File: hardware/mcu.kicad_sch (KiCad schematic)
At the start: 11 parts, among them U0 STM32U575CIT6

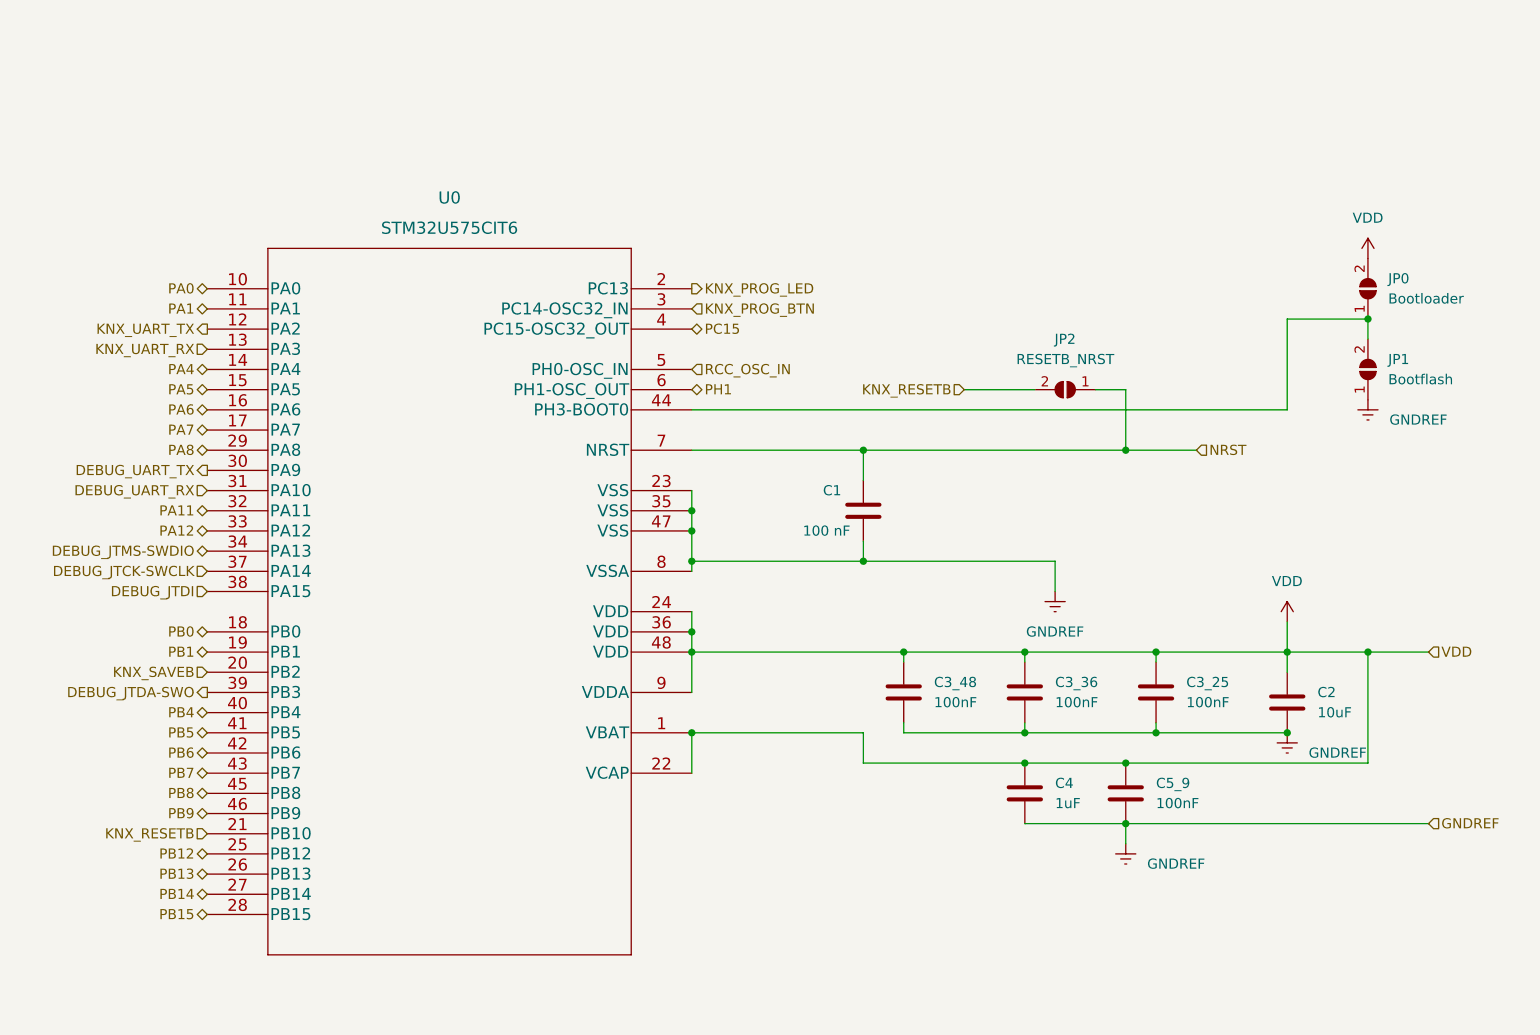
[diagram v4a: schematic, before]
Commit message: Switch to STM32G491KEU6 with NCN5130
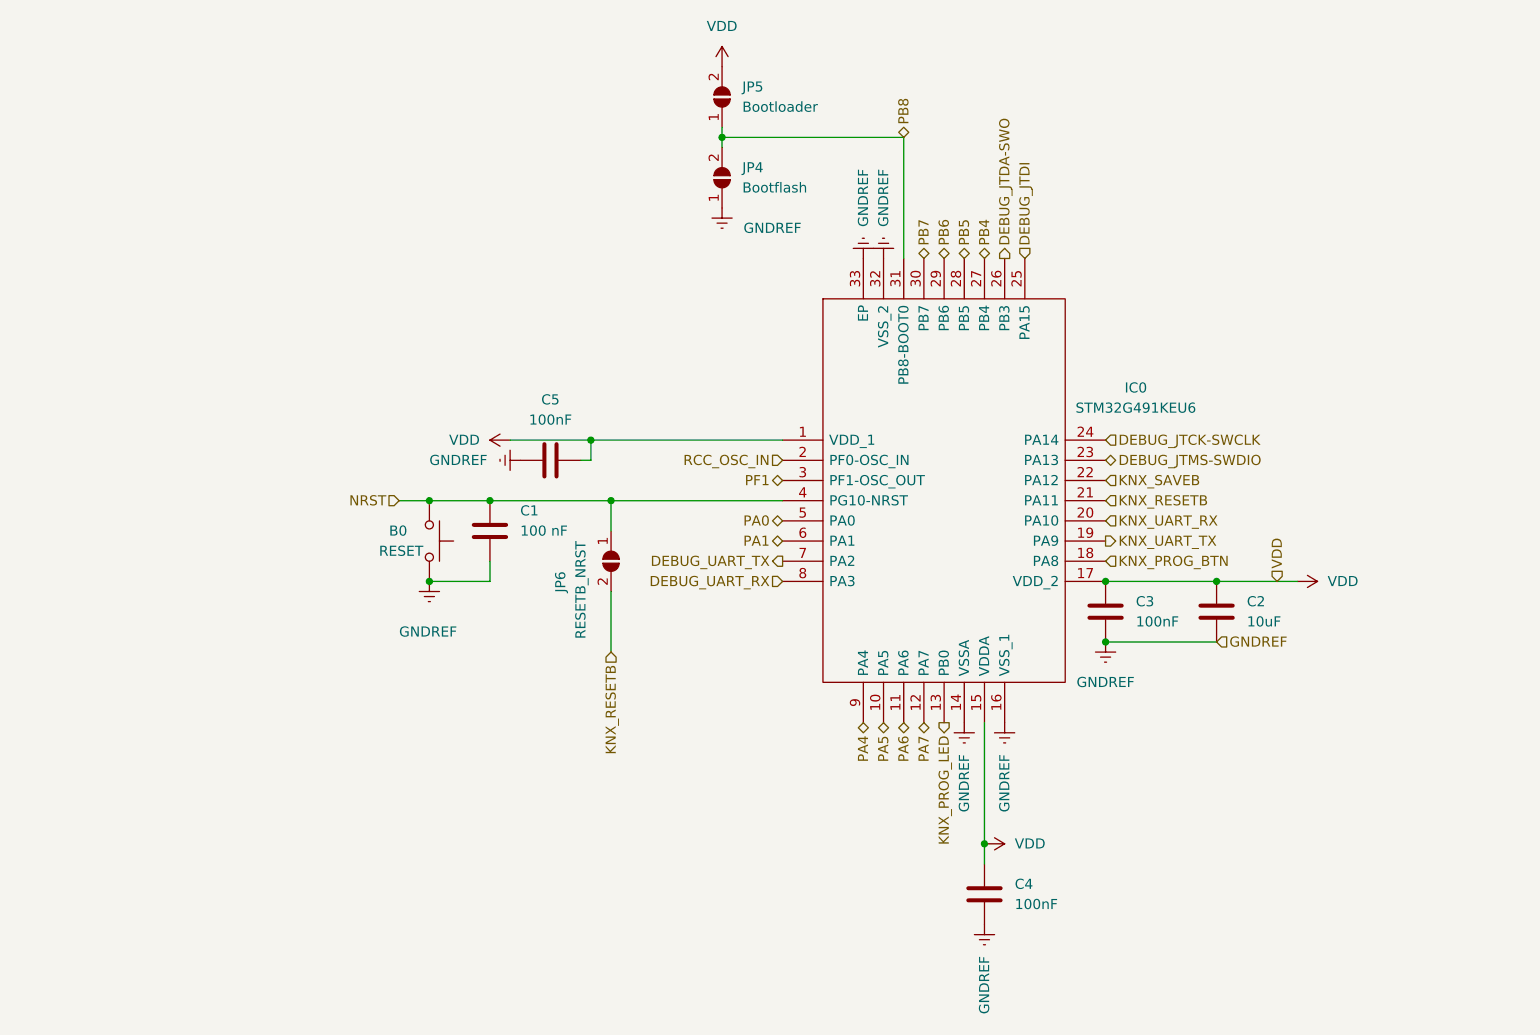
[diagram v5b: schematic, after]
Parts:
- removed C4: 1uF, Capacitor_SMD:C_0603_1608Metric_Pad1.08x0.95mm_HandSolder, symbol Device:C
- removed C5_9: 100nF, Capacitor_SMD:C_0603_1608Metric_Pad1.08x0.95mm_HandSolder, symbol Device:C
- removed JP0: Bootloader, Jumper:SolderJumper-2_P1.3mm_Open_TrianglePad1.0x1.5mm, symbol Jumper:SolderJumper_2_Open
- removed JP1: Bootflash, Jumper:SolderJumper-2_P1.3mm_Open_TrianglePad1.0x1.5mm, symbol Jumper:SolderJumper_2_Open
- removed JP2: RESETB_NRST, Jumper:SolderJumper-2_P1.3mm_Open_TrianglePad1.0x1.5mm, symbol Jumper:SolderJumper_2_Open
- removed U0: STM32U575CIT6, KnxBoard:STM32U575CIT6, symbol STM32U575CIT6:STM32U575CIT6
- added B0: RESET, Button_Switch_SMD:SW_SPST_SKQG_WithStem, symbol Switch:SW_Push
- added IC0: STM32G491KEU6, QFN50P500X500X60-33N-D, symbol STM32G491KEU6:STM32G491KEU6
- added JP4: Bootflash, Jumper:SolderJumper-2_P1.3mm_Open_TrianglePad1.0x1.5mm, symbol Jumper:SolderJumper_2_Open
- added JP5: Bootloader, Jumper:SolderJumper-2_P1.3mm_Open_TrianglePad1.0x1.5mm, symbol Jumper:SolderJumper_2_Open
- added JP6: RESETB_NRST, Jumper:SolderJumper-2_P1.3mm_Open_TrianglePad1.0x1.5mm, symbol Jumper:SolderJumper_2_Open
- renumbered C3_48 to C3, C3_36 to C4, C3_25 to C5
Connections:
- net DEBUG_JTCK-SWCLK: now also IC0.24 (PA14)
- net DEBUG_JTDA-SWO: now also IC0.26 (PB3)
- net DEBUG_JTDI: now also IC0.25 (PA15)
- net DEBUG_JTMS-SWDIO: now also IC0.23 (PA13)
- net DEBUG_UART_RX: now also IC0.8 (PA3)
- net DEBUG_UART_TX: now also IC0.7 (PA2)
- net GNDREF: now also C5.1, B0.2, IC0.14 (VSSA), IC0.16 (VSS_1), IC0.32 (VSS_2), IC0.33 (EP), JP4.1 (A); no longer C5.2
- net KNX_PROG_BTN: now also IC0.18 (PA8)
- net KNX_PROG_LED: now also IC0.13 (PB0)
- net KNX_RESETB: now also IC0.21 (PA11), JP6.2 (B)
- net KNX_SAVEB: now also IC0.22 (PA12)
- net KNX_UART_RX: now also IC0.20 (PA10)
- net KNX_UART_TX: now also IC0.19 (PA9)
- net NRST: now also B0.1, IC0.4 (PG10-NRST), JP6.1 (A)
- net PA0: now also IC0.5 (PA0)
- net PA1: now also IC0.6 (PA1)
- net PA4: now also IC0.9 (PA4)
- net PA5: now also IC0.10 (PA5)
- net PA6: now also IC0.11 (PA6)
- net PA7: now also IC0.12 (PA7)
- net PB4: now also IC0.27 (PB4)
- net PB5: now also IC0.28 (PB5)
- net PB6: now also IC0.29 (PB6)
- net PB7: now also IC0.30 (PB7)
- net PB8: now also IC0.31 (PB8-BOOT0), JP4.2 (B), JP5.1 (A)
- net RCC_OSC_IN: now also IC0.2 (PF0-OSC_IN)
- net VDD: now also C5.2, IC0.1 (VDD_1), IC0.15 (VDDA), IC0.17 (VDD_2), JP5.2 (B); no longer C5.1
- new net PF1: IC0.3 (PF1-OSC_OUT)
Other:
- moved on the sheet: C2, C3, C4, C5

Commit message: Routage OK need check and mass and texts
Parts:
- removed JP4: Bootflash, Jumper:SolderJumper-2_P1.3mm_Open_TrianglePad1.0x1.5mm, symbol Jumper:SolderJumper_2_Open
- removed JP5: Bootloader, Jumper:SolderJumper-2_P1.3mm_Open_TrianglePad1.0x1.5mm, symbol Jumper:SolderJumper_2_Open
- added JP4: BootMode, Jumper:SolderJumper-3_P1.3mm_Open_RoundedPad1.0x1.5mm, symbol Jumper:SolderJumper_3_Bridged12
- renumbered C1 to C20, C5 to C21, C3 to C22, C2 to C23, C4 to C24
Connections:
- net GNDREF: now also JP4.1 (A)
- net PB8: now also JP4.2 (C)
- net VDD: now also JP4.3 (B)
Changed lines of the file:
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@@
   (junction (at 232.41 91.44) (diameter 0) (color 0 0 0 0)
   )
+  (junction (at 203.2 124.46) (diameter 0) (color 0 0 0 0)
+  )
   (junction (at 153.67 73.66) (diameter 0) (color 0 0 0 0)
   )
@@
   (junction (at 218.44 91.44) (diameter 0) (color 0 0 0 0)
   )
-  (junction (at 170.18 35.56) (diameter 0) (color 0 0 0 0)
-  )
   (junction (at 218.44 99.06) (diameter 0) (color 0 0 0 0)
   )
   (junction (at 140.97 81.28) (diameter 0) (color 0 0 0 0)
   )
-  (junction (at 203.2 124.46) (diameter 0) (color 0 0 0 0)
-  )
   (wire (pts (xy 129.54 81.28) (xy 133.35 81.28))
     (stroke (width 0) (type default) (color 0 0 0 0))
   )
-  (wire (pts (xy 170.18 34.29) (xy 170.18 35.56))
-    (stroke (width 0) (type default) (color 0 0 0 0))
-  )
   (wire (pts (xy 133.35 81.28) (xy 140.97 81.28))
     (stroke (width 0) (type default) (color 0 0 0 0))
@@
     (stroke (width 0) (type default) (color 0 0 0 0))
   )
-  (wire (pts (xy 170.18 35.56) (xy 170.18 36.83))
-    (stroke (width 0) (type default) (color 0 0 0 0))
-  )
-  (wire (pts (xy 193.04 35.56) (xy 170.18 35.56))
-    (stroke (width 0) (type default) (color 0 0 0 0))
-  )
   (wire (pts (xy 140.97 91.44) (xy 133.35 91.44))
     (stroke (width 0) (type default) (color 0 0 0 0))
   )
+  (wire (pts (xy 173.99 35.56) (xy 193.04 35.56))
+    (stroke (width 0) (type default) (color 0 0 0 0))
+  )
+  (wire (pts (xy 203.2 124.46) (xy 203.2 127))
+    (stroke (width 0) (type default) (color 0 0 0 0))
+  )
   (wire (pts (xy 140.97 88.9) (xy 140.97 91.44))
     (stroke (width 0) (type default) (color 0 0 0 0))
@@
     (stroke (width 0) (type default) (color 0 0 0 0))
   )
-  (wire (pts (xy 203.2 124.46) (xy 203.2 127))
+  (wire (pts (xy 203.2 109.22) (xy 203.2 124.46))
     (stroke (width 0) (type default) (color 0 0 0 0))
   )
@@
     (stroke (width 0) (type default) (color 0 0 0 0))
   )
-  (wire (pts (xy 203.2 109.22) (xy 203.2 124.46))
-    (stroke (width 0) (type default) (color 0 0 0 0))
-  )
   (wire (pts (xy 156.21 81.28) (xy 156.21 85.09))
     (stroke (width 0) (type default) (color 0 0 0 0))
@@
     (effects (font (size 1.27 1.27)) (justify left))
   )
-  (hierarchical_label "VDD" (shape input) (at 240.03 91.44 90)
-    (effects (font (size 1.27 1.27)) (justify left))
-  )
   (hierarchical_label "DEBUG_JTCK-SWCLK" (shape input) (at 218.44 73.66 0)
     (effects (font (size 1.27 1.27)) (justify left))
   )
-  (hierarchical_label "GNDREF" (shape input) (at 232.41 99.06 0)
-    (effects (font (size 1.27 1.27)) (justify left))
-  )
   (hierarchical_label "DEBUG_JTDI" (shape input) (at 208.28 50.8 90)
     (effects (font (size 1.27 1.27)) (justify left))
@@
   (hierarchical_label "DEBUG_UART_RX" (shape input) (at 177.8 91.44 180)
     (effects (font (size 1.27 1.27)) (justify right))
+  )
+  (symbol (lib_id "power:VDD") (at 203.2 124.46 270) (unit 1)
+    (in_bom yes) (on_board yes)
+    (property "Reference" "#PWR0136" (id 0) (at 199.39 124.46 0)
+      (effects (font (size 1.27 1.27)) hide)
+    )
+    (property "Value" "VDD" (id 1) (at 207.01 124.4599 90)
+      (effects (font (size 1.27 1.27)) (justify left))
+    )
+    (property "Footprint" "" (id 2) (at 203.2 124.46 0)
+      (effects (font (size 1.27 1.27)) hide)
+    )
+    (property "Datasheet" "" (id 3) (at 203.2 124.46 0)
+      (effects (font (size 1.27 1.27)) hide)
+    )
+    (pin "1")
+  )
+  (symbol (lib_id "Jumper:SolderJumper_3_Bridged12") (at 170.18 35.56 90) (unit 1)
+    (in_bom yes) (on_board yes)
+    (property "Reference" "JP4" (id 0) (at 167.64 35.56 0))
+    (property "Value" "BootMode" (id 1) (at 166.37 35.56 0)
+      (effects (font (size 1.27 1.27)) hide)
+    )
+    (property "Footprint" "Jumper:SolderJumper-3_P1.3mm_Open_RoundedPad1.0x1.5mm" (id 2) (at 170.18 35.56 0)
+      (effects (font (size 1.27 1.27)) hide)
+    )
+    (property "Datasheet" "~" (id 3) (at 170.18 35.56 0)
+      (effects (font (size 1.27 1.27)) hide)
+    )
+    (pin "1")
+    (pin "2")
+    (pin "3")
   )
   (symbol (lib_id "power:GNDREF") (at 218.44 99.06 0) (unit 1)
@@
   (symbol (lib_id "Device:C") (at 140.97 85.09 0) (unit 1)
     (in_bom yes) (on_board yes)
-    (property "Reference" "C1" (id 0) (at 144.78 82.55 0)
+    (property "Reference" "C20" (id 0) (at 144.78 82.55 0)
       (effects (font (size 1.27 1.27)) (justify left))
     )
@@
     (pin "1")
   )
-  (symbol (lib_id "power:VDD") (at 203.2 124.46 270) (unit 1)
-    (in_bom yes) (on_board yes) (fields_autoplaced)
-    (property "Reference" "#PWR0136" (id 0) (at 199.39 124.46 0)
-      (effects (font (size 1.27 1.27)) hide)
-    )
-    (property "Value" "VDD" (id 1) (at 207.01 124.4599 90)
-      (effects (font (size 1.27 1.27)) (justify left))
-    )
-    (property "Footprint" "" (id 2) (at 203.2 124.46 0)
-      (effects (font (size 1.27 1.27)) hide)
-    )
-    (property "Datasheet" "" (id 3) (at 203.2 124.46 0)
-      (effects (font (size 1.27 1.27)) hide)
-    )
-    (pin "1")
-  )
   (symbol (lib_id "Device:C") (at 203.2 130.81 0) (unit 1)
     (in_bom yes) (on_board yes) (fields_autoplaced)
-    (property "Reference" "C4" (id 0) (at 207.01 129.5399 0)
+    (property "Reference" "C24" (id 0) (at 207.01 129.5399 0)
       (effects (font (size 1.27 1.27)) (justify left))
     )
@@
     (pin "1")
   )
-  (symbol (lib_id "power:GNDREF") (at 170.18 44.45 0) (unit 1)
-    (in_bom yes) (on_board yes)
-    (property "Reference" "#PWR0134" (id 0) (at 170.18 50.8 0)
-      (effects (font (size 1.27 1.27)) hide)
-    )
-    (property "Value" "GNDREF" (id 1) (at 176.53 46.99 0))
-    (property "Footprint" "" (id 2) (at 170.18 44.45 0)
-      (effects (font (size 1.27 1.27)) hide)
-    )
-    (property "Datasheet" "" (id 3) (at 170.18 44.45 0)
+  (symbol (lib_id "power:GNDREF") (at 170.18 40.64 0) (unit 1)
+    (in_bom yes) (on_board yes)
+    (property "Reference" "#PWR0134" (id 0) (at 170.18 46.99 0)
+      (effects (font (size 1.27 1.27)) hide)
+    )
+    (property "Value" "GNDREF" (id 1) (at 176.53 43.18 0))
+    (property "Footprint" "" (id 2) (at 170.18 40.64 0)
+      (effects (font (size 1.27 1.27)) hide)
+    )
+    (property "Datasheet" "" (id 3) (at 170.18 40.64 0)
       (effects (font (size 1.27 1.27)) hide)
     )
@@
     )
     (property "Datasheet" "~" (id 3) (at 156.21 88.9 0)
-      (effects (font (size 1.27 1.27)) hide)
-    )
-    (pin "1")
-    (pin "2")
-  )
-  (symbol (lib_id "Jumper:SolderJumper_2_Open") (at 170.18 40.64 90) (unit 1)
-    (in_bom yes) (on_board yes) (fields_autoplaced)
-    (property "Reference" "JP4" (id 0) (at 172.72 39.3699 90)
-      (effects (font (size 1.27 1.27)) (justify right))
-    )
-    (property "Value" "Bootflash" (id 1) (at 172.72 41.9099 90)
-      (effects (font (size 1.27 1.27)) (justify right))
-    )
-    (property "Footprint" "Jumper:SolderJumper-2_P1.3mm_Open_TrianglePad1.0x1.5mm" (id 2) (at 170.18 40.64 0)
-      (effects (font (size 1.27 1.27)) hide)
-    )
-    (property "Datasheet" "~" (id 3) (at 170.18 40.64 0)
       (effects (font (size 1.27 1.27)) hide)
     )
@@
   (symbol (lib_id "Device:C") (at 148.59 76.2 90) (unit 1)
     (in_bom yes) (on_board yes) (fields_autoplaced)
-    (property "Reference" "C5" (id 0) (at 148.59 68.58 90))
+    (property "Reference" "C21" (id 0) (at 148.59 68.58 90))
     (property "Value" "100nF" (id 1) (at 148.59 71.12 90))
     (property "Footprint" "Capacitor_SMD:C_0603_1608Metric_Pad1.08x0.95mm_HandSolder" (id 2) (at 152.4 75.2348 0)
@@
     (pin "1")
   )
-  (symbol (lib_id "Jumper:SolderJumper_2_Open") (at 170.18 30.48 90) (unit 1)
-    (in_bom yes) (on_board yes) (fields_autoplaced)
-    (property "Reference" "JP5" (id 0) (at 172.72 29.2099 90)
-      (effects (font (size 1.27 1.27)) (justify right))
-    )
-    (property "Value" "Bootloader" (id 1) (at 172.72 31.7499 90)
-      (effects (font (size 1.27 1.27)) (justify right))
-    )
-    (property "Footprint" "Jumper:SolderJumper-2_P1.3mm_Open_TrianglePad1.0x1.5mm" (id 2) (at 170.18 30.48 0)
-      (effects (font (size 1.27 1.27)) hide)
-    )
-    (property "Datasheet" "~" (id 3) (at 170.18 30.48 0)
-      (effects (font (size 1.27 1.27)) hide)
-    )
-    (pin "1")
-    (pin "2")
-  )
   (symbol (lib_id "Device:C") (at 232.41 95.25 0) (unit 1)
     (in_bom yes) (on_board yes) (fields_autoplaced)
-    (property "Reference" "C2" (id 0) (at 236.22 93.9799 0)
+    (property "Reference" "C23" (id 0) (at 236.22 93.9799 0)
       (effects (font (size 1.27 1.27)) (justify left))
     )
@@
   (symbol (lib_id "Device:C") (at 218.44 95.25 0) (unit 1)
     (in_bom yes) (on_board yes) (fields_autoplaced)
-    (property "Reference" "C3" (id 0) (at 222.25 93.9799 0)
+    (property "Reference" "C22" (id 0) (at 222.25 93.9799 0)
       (effects (font (size 1.27 1.27)) (justify left))
     )
@@
     (pin "1")
   )
-  (symbol (lib_id "power:VDD") (at 170.18 26.67 0) (unit 1)
-    (in_bom yes) (on_board yes) (fields_autoplaced)
-    (property "Reference" "#PWR0135" (id 0) (at 170.18 30.48 0)
-      (effects (font (size 1.27 1.27)) hide)
-    )
-    (property "Value" "VDD" (id 1) (at 170.18 21.59 0))
-    (property "Footprint" "" (id 2) (at 170.18 26.67 0)
-      (effects (font (size 1.27 1.27)) hide)
-    )
-    (property "Datasheet" "" (id 3) (at 170.18 26.67 0)
-      (effects (font (size 1.27 1.27)) hide)
-    )
+  (symbol (lib_id "power:VDD") (at 170.18 30.48 0) (unit 1)
+    (in_bom yes) (on_board yes) (fields_autoplaced)
+    (property "Reference" "#PWR0135" (id 0) (at 170.18 34.29 0)
+      (effects (font (size 1.27 1.27)) hide)
+    )
+    (property "Value" "VDD" (id 1) (at 170.18 25.4 0))
+    (property "Footprint" "" (id 2) (at 170.18 30.48 0)
+      (effects (font (size 1.27 1.27)) hide)
+    )
+    (property "Datasheet" "" (id 3) (at 170.18 30.48 0)
+      (effects (font (size 1.27 1.27)) hide)
+    )

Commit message: Seed SeeedStudio N°1
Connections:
- net DEBUG_JTDA-SWO renamed PB3
- net DEBUG_JTDI renamed PA15
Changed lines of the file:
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@@
     (effects (font (size 1.27 1.27)) (justify left))
   )
-  (hierarchical_label "DEBUG_JTDI" (shape input) (at 208.28 50.8 90)
+  (hierarchical_label "PA15" (shape bidirectional) (at 208.28 50.8 90)
     (effects (font (size 1.27 1.27)) (justify left))
   )
@@
     (effects (font (size 1.27 1.27)) (justify right))
   )
-  (hierarchical_label "DEBUG_JTDA-SWO" (shape output) (at 205.74 50.8 90)
+  (hierarchical_label "PB3" (shape bidirectional) (at 205.74 50.8 90)
     (effects (font (size 1.27 1.27)) (justify left))
   )
